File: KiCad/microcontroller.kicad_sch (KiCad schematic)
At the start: 57 parts, among them J4 Debugger, SW1 Reset switch, U7 24LC256

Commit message: footprint added
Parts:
- D4, D5: footprint (none) -> footprint:LED0603-RD
- J3: footprint (none) -> footprint:HDR-TH_24P-P2.54-V-F
- J4: footprint (none) -> footprint:HDR-TH_3P-P2.54_CS-1165SDIG
- R11: footprint (none) -> footprint:R0402
- R11, R30, R31, R32, R33, R34, R35, R36, R37, R38, R39, R40, R41, R42, R43, R44, R45, R46, R47, R69, R70, R71, R72: footprint (none) -> footprint:R0603
- R56, R57: footprint (none) -> footprint:R0805; JLC code C19702 -> C17630; Part name 0603WAF1201T5E -> 0805W8F3300T5E; cost per unit 0,0066 -> 0,0016
- R64: footprint (none) -> footprint:R0805
- SW1: footprint (none) -> footprint:SW-SMD_4P-L5.1-W5.1-P3.70-LS6.5-TL-2
- SW2, SW3, SW4: value ~ -> switch; footprint (none) -> footprint:SW-SMD_4P-L5.1-W5.1-P3.70-LS6.5-TL-2
- TP10: footprint (none) -> TestPoint:TestPoint_Loop_D2.54mm_Drill1.5mm_Beaded
- TP10: value STM BOOT0 -> STM32 BOOT0; footprint (none) -> TestPoint:TestPoint_Loop_D2.54mm_Drill1.5mm_Beaded
- TP10: value STM32 output -> STM32 LED2; footprint (none) -> TestPoint:TestPoint_Loop_D2.54mm_Drill1.5mm_Beaded
- TP10: value STM32 output -> STM32 LED1; footprint (none) -> TestPoint:TestPoint_Loop_D2.54mm_Drill1.5mm_Beaded
- U7: footprint (none) -> footprint:PDIP-8_L9.3-W6.4-P2.54-LS7.6-BL

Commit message: gerber power changed
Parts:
- J3: footprint footprint:HDR-TH_24P-P2.54-V-F -> footprint:STM32F051C6_female_header
- TP10: footprint TestPoint:TestPoint_Loop_D2.54mm_Drill1.5mm_Beaded -> footprint:Testpoint_2.54mm
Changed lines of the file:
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@@
       (effects (font (size 1.27 1.27)) (justify left))
     )
-    (property "Footprint" "TestPoint:TestPoint_Loop_D2.54mm_Drill1.5mm_Beaded" (at 240.03 72.39 0)
+    (property "Footprint" "footprint:Testpoint_2.54mm" (at 240.03 72.39 0)
       (effects (font (size 1.27 1.27)) hide)
     )
@@
       (effects (font (size 1.27 1.27)) (justify left))
     )
-    (property "Footprint" "TestPoint:TestPoint_Loop_D2.54mm_Drill1.5mm_Beaded" (at 45.72 73.66 0)
+    (property "Footprint" "footprint:Testpoint_2.54mm" (at 45.72 73.66 0)
       (effects (font (size 1.27 1.27)) hide)
     )
@@
       (effects (font (size 1.27 1.27)) (justify left))
     )
-    (property "Footprint" "TestPoint:TestPoint_Loop_D2.54mm_Drill1.5mm_Beaded" (at 118.872 39.624 0)
+    (property "Footprint" "footprint:Testpoint_2.54mm" (at 118.872 39.624 0)
       (effects (font (size 1.27 1.27)) hide)
     )
@@
       (effects (font (size 1.27 1.27)) (justify left))
     )
-    (property "Footprint" "TestPoint:TestPoint_Loop_D2.54mm_Drill1.5mm_Beaded" (at 45.72 67.31 0)
+    (property "Footprint" "footprint:Testpoint_2.54mm" (at 45.72 67.31 0)
       (effects (font (size 1.27 1.27)) hide)
     )
@@
       (effects (font (size 1.27 1.27)) (justify left))
     )
-    (property "Footprint" "TestPoint:TestPoint_Loop_D2.54mm_Drill1.5mm_Beaded" (at 40.64 45.72 0)
+    (property "Footprint" "footprint:Testpoint_2.54mm" (at 40.64 45.72 0)
       (effects (font (size 1.27 1.27)) hide)
     )
@@
       (effects (font (size 1.27 1.27)))
     )
-    (property "Footprint" "TestPoint:TestPoint_Loop_D2.54mm_Drill1.5mm_Beaded" (at 186.69 149.86 0)
+    (property "Footprint" "footprint:Testpoint_2.54mm" (at 186.69 149.86 0)
       (effects (font (size 1.27 1.27)) hide)
     )
@@
       (effects (font (size 1.27 1.27)) (justify left))
     )
-    (property "Footprint" "TestPoint:TestPoint_Loop_D2.54mm_Drill1.5mm_Beaded" (at 121.158 178.562 0)
+    (property "Footprint" "footprint:Testpoint_2.54mm" (at 121.158 178.562 0)
       (effects (font (size 1.27 1.27)) hide)
     )
@@
       (effects (font (size 1.27 1.27)) (justify left))
     )
-    (property "Footprint" "TestPoint:TestPoint_Loop_D2.54mm_Drill1.5mm_Beaded" (at 250.19 68.58 0)
+    (property "Footprint" "footprint:Testpoint_2.54mm" (at 250.19 68.58 0)
       (effects (font (size 1.27 1.27)) hide)
     )
@@
       (effects (font (size 1.27 1.27)))
     )
-    (property "Footprint" "footprint:HDR-TH_24P-P2.54-V-F" (at 144.272 71.374 0)
+    (property "Footprint" "footprint:STM32F051C6_female_header" (at 144.272 71.374 0)
       (effects (font (size 1.27 1.27)) hide)
     )
@@
       (effects (font (size 1.27 1.27)) (justify left))
     )
-    (property "Footprint" "TestPoint:TestPoint_Loop_D2.54mm_Drill1.5mm_Beaded" (at 120.65 166.37 0)
+    (property "Footprint" "footprint:Testpoint_2.54mm" (at 120.65 166.37 0)
       (effects (font (size 1.27 1.27)) hide)
     )
@@
       (effects (font (size 1.27 1.27)) (justify left))
     )
-    (property "Footprint" "TestPoint:TestPoint_Loop_D2.54mm_Drill1.5mm_Beaded" (at 267.97 106.68 0)
+    (property "Footprint" "footprint:Testpoint_2.54mm" (at 267.97 106.68 0)
       (effects (font (size 1.27 1.27)) hide)
     )
@@
       (effects (font (size 1.27 1.27)) (justify left))
     )
-    (property "Footprint" "TestPoint:TestPoint_Loop_D2.54mm_Drill1.5mm_Beaded" (at 266.7 101.6 0)
+    (property "Footprint" "footprint:Testpoint_2.54mm" (at 266.7 101.6 0)
       (effects (font (size 1.27 1.27)) hide)
     )
@@
       (effects (font (size 1.27 1.27)))
     )
-    (property "Footprint" "TestPoint:TestPoint_Loop_D2.54mm_Drill1.5mm_Beaded" (at 165.862 30.734 0)
+    (property "Footprint" "footprint:Testpoint_2.54mm" (at 165.862 30.734 0)
       (effects (font (size 1.27 1.27)) hide)
     )
@@
       (effects (font (size 1.27 1.27)) (justify left))
     )
-    (property "Footprint" "TestPoint:TestPoint_Loop_D2.54mm_Drill1.5mm_Beaded" (at 45.72 80.01 0)
-      (effects (font (size 1.27 1.27)) hide)
-    )
+    (property "Footprint" "footprint:Testpoint_2.54mm" (at 45.72 80.01 0)
+      (effects (font (size 1.27 1.27)) hide)
+    )

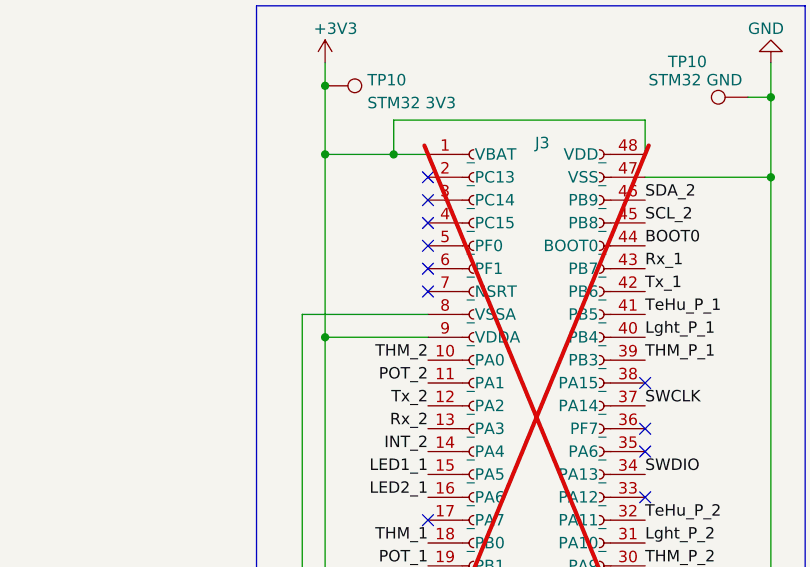
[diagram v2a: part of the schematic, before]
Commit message: the PCB suffered - wired up the micro controller
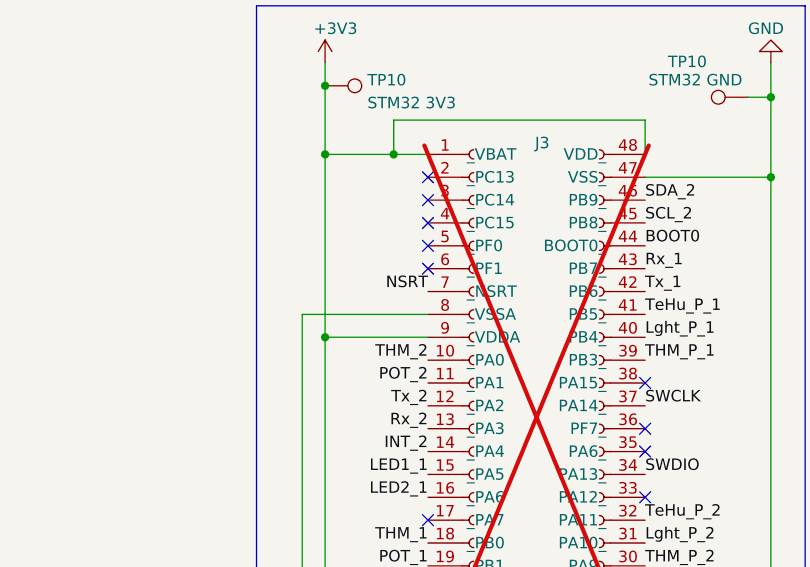
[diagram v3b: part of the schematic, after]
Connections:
- net NSRT: now also J3.7 (_NSRT)
- no-connect marks 11 -> 10
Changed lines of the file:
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@@
   (no_connect (at 154.432 80.264))
   (no_connect (at 130.302 82.804))
-  (no_connect (at 130.302 57.404))
   (no_connect (at 130.302 49.784))
   (no_connect (at 154.432 75.184))
@@
     (effects (font (size 1.27 1.27)) (justify right bottom))
   )
+  (label "NSRT" (at 130.302 57.404 180) (fields_autoplaced)
+    (effects (font (size 1.27 1.27)) (justify right bottom))
+  )

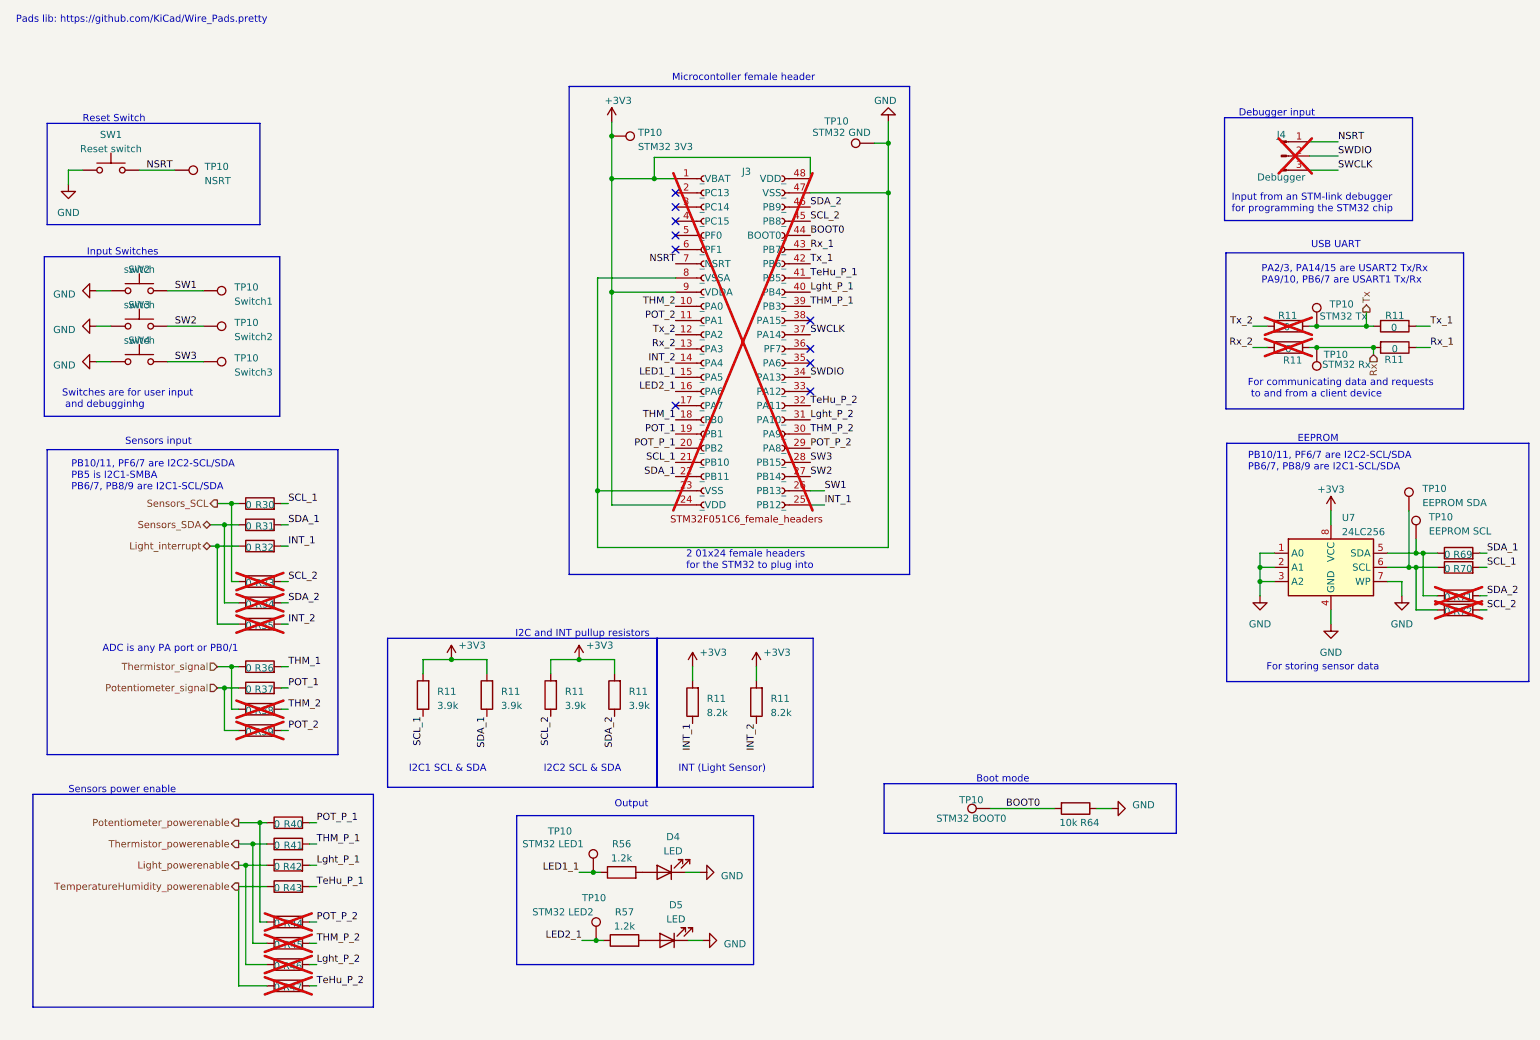
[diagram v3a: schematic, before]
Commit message: powwer 5v line seperation
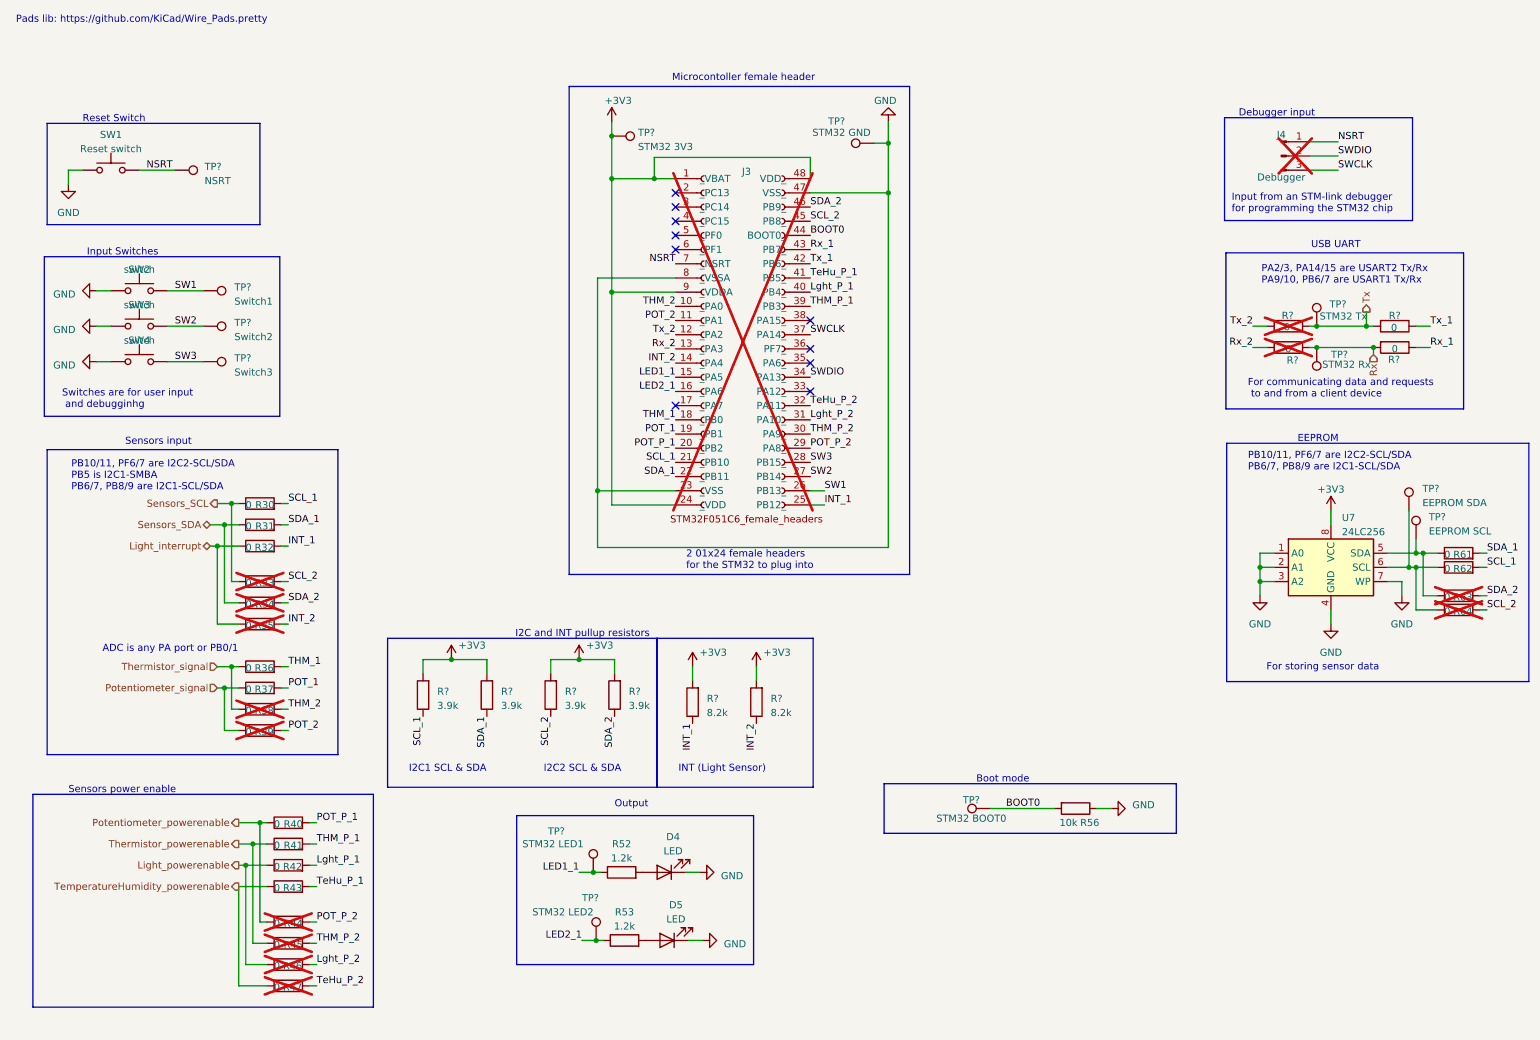
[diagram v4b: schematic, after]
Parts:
- renumbered R56 to R52, R57 to R53, R64 to R56, R69 to R61, R70 to R62, R71 to R63, R72 to R64, R11 to R?, TP10 to TP?

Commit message: Removed extra 0ohms, added microcontroller male header
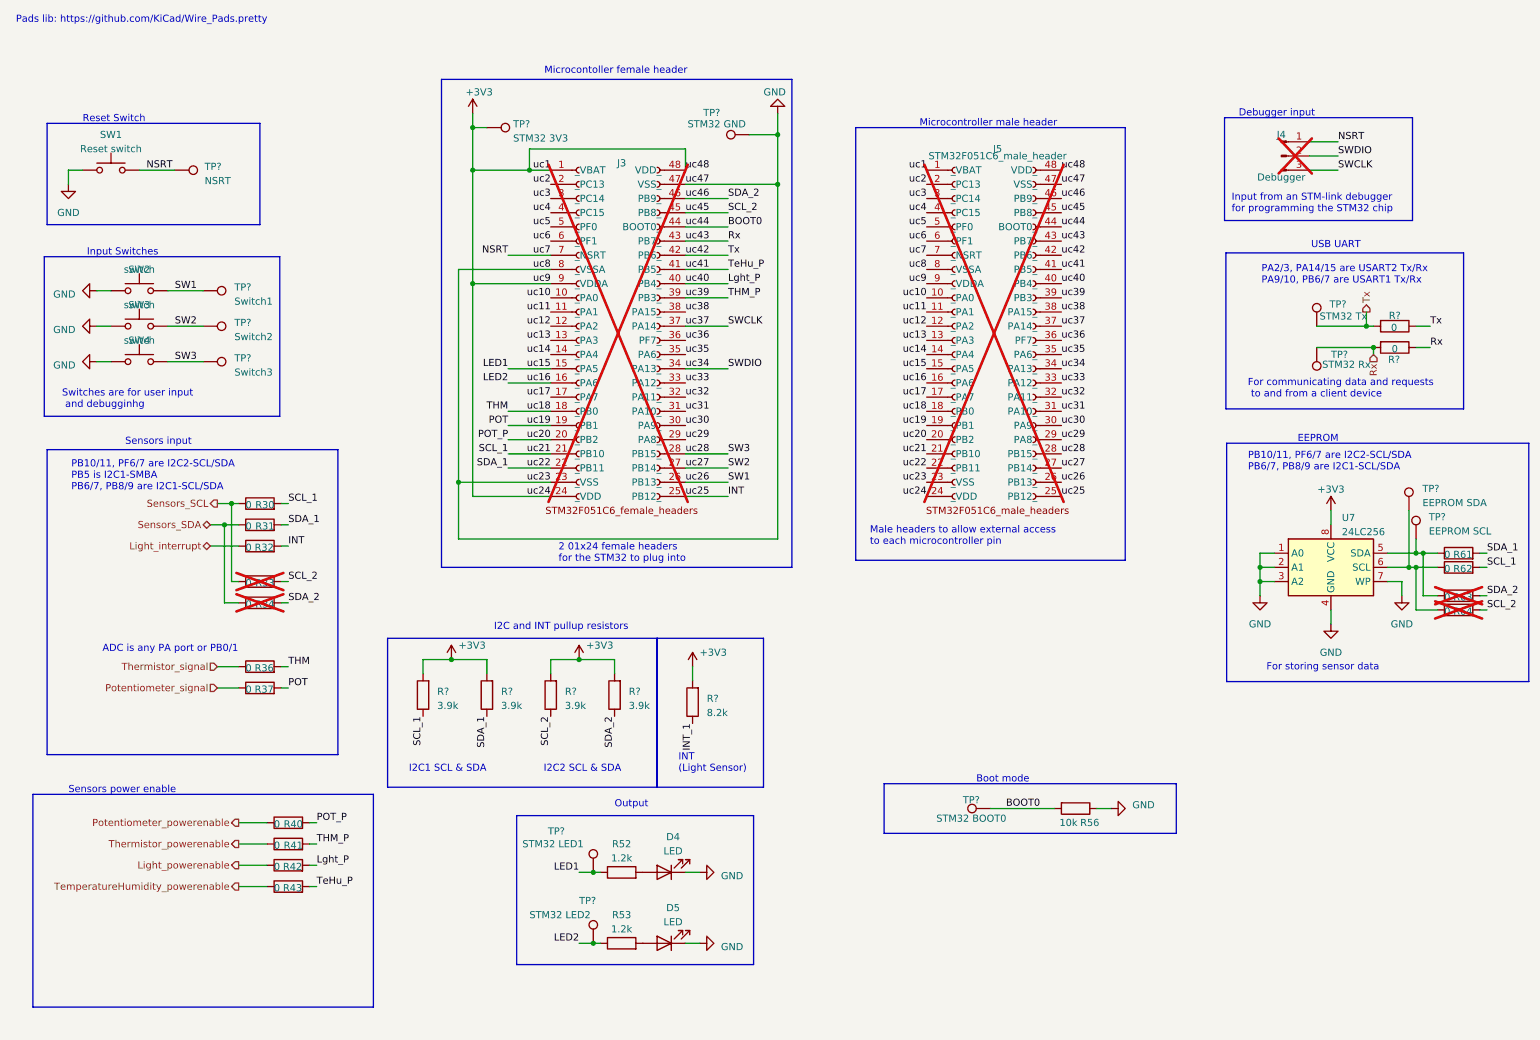
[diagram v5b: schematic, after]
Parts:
- removed R35, R38, R39, R44, R45, R46, R47, R? (x2): 0, footprint:R0603, symbol Device:R
- removed R?: 8.2k, footprint:R0402, symbol Device:R
- added J5: STM32F051C6_male_header, symbol EEE3088F_CKR:STM32F051C6_male_header
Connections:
- net Rx_1 is gone; now on net Rx: J3.43 (PB7_), R?.1
- net Tx_1 is gone; now on net Tx: J3.42 (PB6_), R?.1
- net +3V3: now also J5.1 (_VBAT), J5.24 (_VDD), J5.48 (VDD_), J5.9 (_VDDA)
- net BOOT0: now also J5.44 (BOOT0_)
- net GND: now also J5.23 (_VSS), J5.47 (VSS_), J5.8 (_VSSA)
- net INT_1: no longer J3.25 (PB12_), R32.2
- net NSRT: now also J5.7 (_NSRT)
- net Rx: now also J5.43 (PB7_)
- net SCL_1: now also J5.21 (_PB10)
- net SCL_2: now also J5.45 (PB8_)
- net SDA_1: now also J5.22 (_PB11)
- net SDA_2: now also J5.46 (PB9_)
- net SW1: now also J5.26 (PB13_)
- net SW2: now also J5.27 (PB14_)
- net SW3: now also J5.28 (PB15_)
- net SWCLK: now also J5.37 (PA14_)
- net SWDIO: now also J5.34 (PA13_)
- net Tx: now also J5.42 (PB6_)
- net uc17: now reaches J3.17 (_PA7)
- net uc17: now also J5.17 (_PA7)
- net uc2: now reaches J3.2 (_PC13)
- net uc2: now also J5.2 (_PC13)
- net uc3: now reaches J3.3 (_PC14)
- net uc3: now also J5.3 (_PC14)
- net uc33: now reaches J3.33 (PA12_)
- net uc33: now also J5.33 (PA12_)
- net uc35: now reaches J3.35 (PA6_)
- net uc35: now also J5.35 (PA6_)
- net uc36: now reaches J3.36 (PF7_)
- net uc36: now also J5.36 (PF7_)
- net uc38: now reaches J3.38 (PA15_)
- net uc38: now also J5.38 (PA15_)
- net uc4: now reaches J3.4 (_PC15)
- net uc4: now also J5.4 (_PC15)
- net uc5: now reaches J3.5 (_PF0)
- net uc5: now also J5.5 (_PF0)
- net uc6: now reaches J3.6 (_PF1)
- net uc6: now also J5.6 (_PF1)
- net INT_2 renamed uc14
- net uc14: now also J5.14 (_PA4)
- net LED1_1 renamed LED1
- net LED1: now also J5.15 (_PA5)
- net LED2_1 renamed LED2
- net LED2: now also J5.16 (_PA6)
- net Lght_P_1 renamed Lght_P
- net Lght_P: now also J5.40 (PB4_)
- net Lght_P_2 renamed uc31
- net uc31: now also J5.31 (PA10_)
- net POT_1 renamed POT
- net POT: now also J5.19 (_PB1)
- net POT_2 renamed uc11
- net uc11: now also J5.11 (_PA1)
- net POT_P_1 renamed POT_P
- net POT_P: now also J5.20 (_PB2)
- net POT_P_2 renamed uc29
- net uc29: now also J5.29 (PA8_)
- net Rx_2 renamed uc13
- net uc13: now also J5.13 (_PA3)
- net THM_1 renamed THM
- net THM: now also J5.18 (_PB0)
- net THM_2 renamed uc10
- net uc10: now also J5.10 (_PA0)
- net THM_P_1 renamed THM_P
- net THM_P: now also J5.39 (PB3_)
- net THM_P_2 renamed uc30
- net uc30: now also J5.30 (PA9_)
- net TeHu_P_1 renamed TeHu_P
- net TeHu_P: now also J5.41 (PB5_)
- net TeHu_P_2 renamed uc32
- net uc32: now also J5.32 (PA11_)
- net Tx_2 renamed uc12
- net uc12: now also J5.12 (_PA2)
- new net INT: J3.25 (PB12_), J5.25 (PB12_), R32.2
- no-connect marks 10 -> 0
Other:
- note added: "Male headers to allow external access to each microcontroller pin"
- note added: "Microcontroller male header"
- moved on the sheet: D5, J3, R53, TP?
